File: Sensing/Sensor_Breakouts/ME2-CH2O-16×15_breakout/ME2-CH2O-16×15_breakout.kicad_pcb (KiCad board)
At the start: 2 copper layers, 15.1 x 26.2 mm, 8 parts, among them J1 Conn_01x03_Pin, U1 ME2-CH2O-16×15, U2 LT6003HS5TRPBF

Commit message: Corrected formaldahyde sensor polarity
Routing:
- net Net-(U1-Working): track 15.9 -> 31.9 mm
- net GND: track 21.8 -> 20.3 mm
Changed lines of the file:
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@@
 			(layer "Dwgs.User")
 			(pts
-				(xy 175.9 78.48) (xy 175.9 70.28)
+				(xy 184.575 64.705) (xy 174.425 64.705)
 			)
-			(height -5.4)
-			(orientation 1)
+			(height -2.925)
+			(orientation 0)
 			(format
 				(prefix "")
@@
 				(keep_text_aligned yes)
 			)
-			(gr_text "8.2"
-				(at 169.4 74.38 90)
+			(gr_text "10.15"
+				(at 179.5 60.68 0)
 				(layer "Dwgs.User")
 				(effects
@@
 			(layer "Dwgs.User")
 			(pts
-				(xy 175.9 78.48) (xy 183.1 78.48)
+				(xy 175.9 78.48) (xy 175.9 70.28)
 			)
-			(height 2.8)
-			(orientation 0)
+			(height -5.4)
+			(orientation 1)
 			(format
 				(prefix "")
@@
 				(keep_text_aligned yes)
 			)
-			(gr_text "7.2"
-				(at 179.5 80.18 0)
+			(gr_text "8.2"
+				(at 169.4 74.38 90)
 				(layer "Dwgs.User")
 				(effects
@@
 			(layer "Dwgs.User")
 			(pts
-				(xy 184.575 64.705) (xy 174.425 64.705)
+				(xy 184.575 75.855) (xy 184.575 64.705)
 			)
-			(height -2.925)
-			(orientation 0)
+			(height 3.925)
+			(orientation 1)
 			(format
 				(prefix "")
@@
 				(keep_text_aligned yes)
 			)
-			(gr_text "10.15"
-				(at 179.5 60.68 0)
+			(gr_text "11.15"
+				(at 187.4 70.28 90)
 				(layer "Dwgs.User")
 				(effects
@@
 			(layer "Dwgs.User")
 			(pts
-				(xy 184.575 75.855) (xy 184.575 64.705)
+				(xy 175.9 78.48) (xy 183.1 78.48)
 			)
-			(height 3.925)
-			(orientation 1)
+			(height 2.8)
+			(orientation 0)
 			(format
 				(prefix "")
@@
 				(keep_text_aligned yes)
 			)
-			(gr_text "11.15"
-				(at 187.4 70.28 90)
+			(gr_text "7.2"
+				(at 179.5 80.18 0)
 				(layer "Dwgs.User")
 				(effects
@@
 			(layers "*.Cu" "*.Mask")
 		)
-		(pad "1" thru_hole roundrect
-			(at -3.6 8.2)
+		(pad "1" thru_hole rect
+			(at 3.6 8.24)
 			(size 3 2.5)
 			(drill oval 2 1.5)
 			(layers "*.Cu" "*.Mask")
 			(remove_unused_layers no)
-			(roundrect_rratio 0.1968503937)
 			(net 1 "Net-(U1-Working)")
 			(pinfunction "Working")
@@
 		)
 		(pad "2" thru_hole rect
-			(at 3.6 8.24)
+			(at -3.6 8.2)
 			(size 3 2.5)
 			(drill oval 2 1.5)
@@
 	)
 	(segment
+		(start 179.292 78.52)
+		(end 178.5875 77.8155)
+		(width 0.2)
+		(layer "F.Cu")
+		(net 1)
+	)
+	(segment
 		(start 173.049 85.2115)
 		(end 173.049 82.951)
@@
 	)
 	(segment
+		(start 173.886108 74.554)
+		(end 173.124 75.316108)
+		(width 0.2)
+		(layer "F.Cu")
+		(net 1)
+	)
+	(segment
 		(start 174.3375 86.5)
 		(end 174.3375 87.95)
@@
 	)
 	(segment
-		(start 178.5875 82)
-		(end 178.5875 81.1675)
+		(start 173.124 81.124)
+		(end 174 82)
 		(width 0.2)
 		(layer "F.Cu")
@@
 	)
 	(segment
-		(start 178.5875 81.1675)
-		(end 175.9 78.48)
+		(start 182.0675 78.52)
+		(end 178.5875 82)
 		(width 0.2)
 		(layer "F.Cu")
@@
 	)
 	(segment
-		(start 174 80.38)
-		(end 175.9 78.48)
+		(start 183.1 78.52)
+		(end 179.292 78.52)
+		(width 0.2)
+		(layer "F.Cu")
+		(net 1)
+	)
+	(segment
+		(start 173.124 75.316108)
+		(end 173.124 81.124)
 		(width 0.2)
 		(layer "F.Cu")
@@
 	)
 	(segment
-		(start 174 82)
-		(end 174 80.38)
+		(start 178.5875 77.8155)
+		(end 175.326 74.554)
+		(width 0.2)
+		(layer "F.Cu")
+		(net 1)
+	)
+	(segment
+		(start 183.1 78.52)
+		(end 182.0675 78.52)
+		(width 0.2)
+		(layer "F.Cu")
+		(net 1)
+	)
+	(segment
+		(start 175.326 74.554)
+		(end 173.886108 74.554)
 		(width 0.2)
 		(layer "F.Cu")
@@
 	)
 	(segment
-		(start 185.1925 82.1375)
-		(end 185.33 82)
-		(width 0.2)
-		(layer "F.Cu")
-		(net 4)
-	)
-	(segment
 		(start 176.4 82)
 		(end 176.4 82.1)
@@
 	)
 	(segment
-		(start 184.25 82.1375)
-		(end 185.1925 82.1375)
+		(start 176.4 78.98)
+		(end 175.9 78.48)
 		(width 0.2)
 		(layer "F.Cu")
@@
 	)
 	(segment
-		(start 185.33 83.5)
-		(end 185.33 82)
-		(width 0.4)
+		(start 176.4 82.1)
+		(end 177.25 82.95)
+		(width 0.2)
 		(layer "F.Cu")
 		(net 4)
 	)
 	(segment
-		(start 176.4 82.1)
-		(end 177.25 82.95)
+		(start 176.4 82)
+		(end 176.4 78.98)
 		(width 0.2)
 		(layer "F.Cu")
@@
 	)
 	(segment
-		(start 185.33 82)
-		(end 185.33 80.75)
-		(width 0.4)
+		(start 185.33 83.2175)
+		(end 184.25 82.1375)
+		(width 0.2)
 		(layer "F.Cu")
 		(net 4)
@@
 	)
 	(segment
-		(start 185.33 80.75)
-		(end 183.1 78.52)
-		(width 0.4)
+		(start 185.33 87.75)
+		(end 185.33 83.2175)
+		(width 0.2)
 		(layer "F.Cu")
 		(net 4)
@@
 		(layer "F.Cu")
 		(net 4)
-	)
-	(segment
-		(start 185.33 87.75)
-		(end 185.33 83.5)
-		(width 0.4)
-		(layer "F.Cu")
-		(net 4)

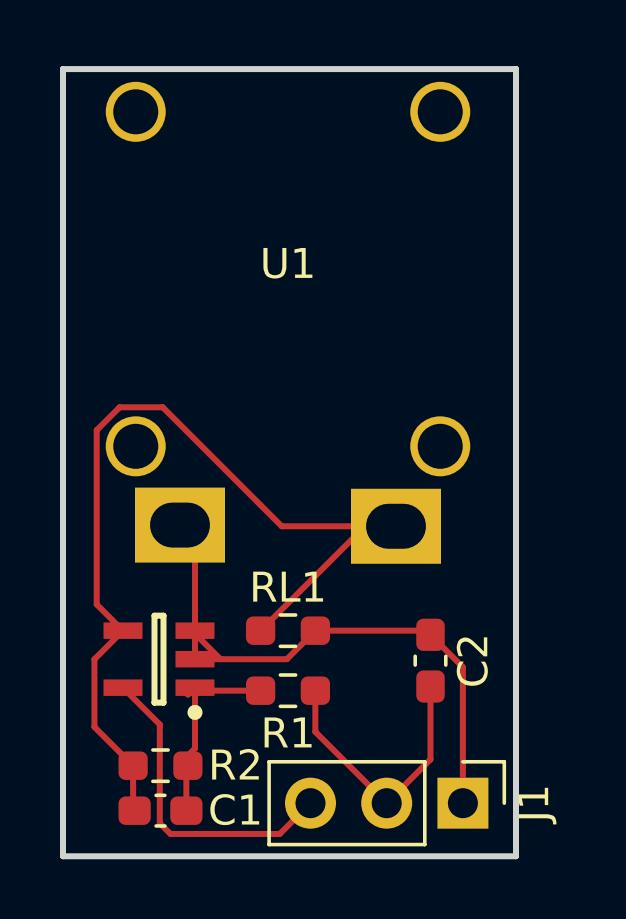
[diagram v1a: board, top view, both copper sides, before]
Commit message: Made small changes to Formaldehyde Sensor
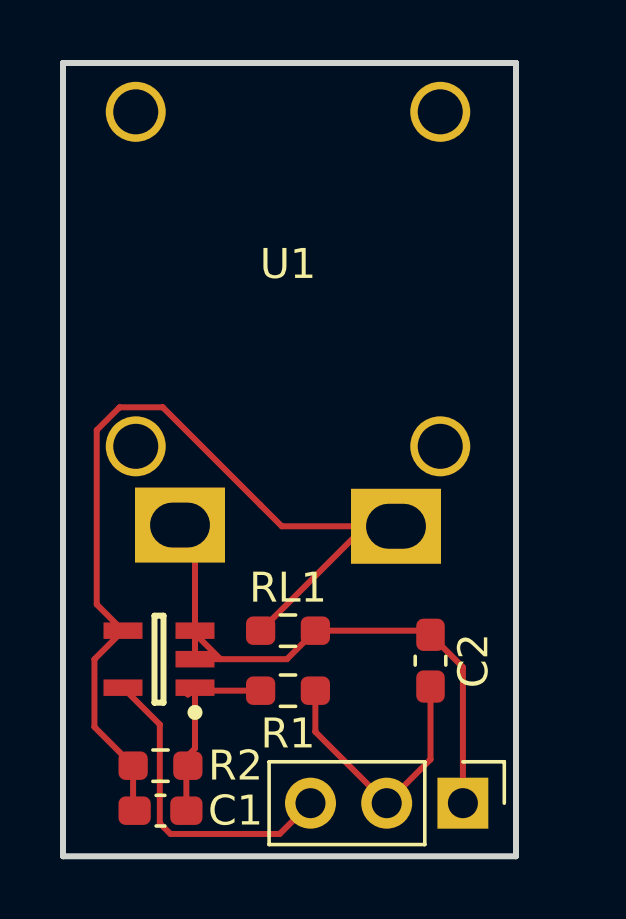
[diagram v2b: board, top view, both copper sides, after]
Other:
- board size 15.1 x 26.2 mm -> 15.1 x 26.4 mm
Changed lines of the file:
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@@
 			(at 0 -2.38 90)
 			(layer "F.SilkS")
+			(hide yes)
 			(effects
 				(font
@@
 	)
 	(gr_rect
-		(start 172 63.28)
+		(start 172 63.077396)
 		(end 187.1 89.52)
 		(stroke
